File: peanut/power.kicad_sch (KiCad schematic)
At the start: 23 parts, among them J4 Battery JST, J5 Arming, Q5 PMOS, U2 TPS2116DRL, U3 LM3671MF

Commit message: Assigned some actual parts and footprints to symbols.
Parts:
- C10: renamed from C5; footprint (none) -> Capacitor_SMD:C_0402_1005Metric
- C11: renamed from C3; footprint (none) -> Capacitor_SMD:C_0402_1005Metric
- C12: renamed from C1; footprint (none) -> Capacitor_SMD:C_0402_1005Metric
- C13: renamed from C2; footprint (none) -> Capacitor_SMD:C_0402_1005Metric
- C9: renamed from C4; footprint (none) -> Capacitor_SMD:C_0402_1005Metric
- D5: footprint (none) -> LED_SMD:LED_0402_1005Metric
- J4: renamed from J5; footprint (none) -> TerminalBlock_Phoenix:TerminalBlock_Phoenix_MPT-0,5-2-2.54_1x02_P2.54mm_Horizontal
- R21: renamed from R14; footprint (none) -> Resistor_SMD:R_0402_1005Metric
- R22: renamed from R17; footprint (none) -> Resistor_SMD:R_0402_1005Metric
- R23: renamed from R15; footprint (none) -> Resistor_SMD:R_0402_1005Metric
- R24: renamed from R13; footprint (none) -> Resistor_SMD:R_0402_1005Metric
- R25: renamed from R16; footprint (none) -> Resistor_SMD:R_0402_1005Metric
- TP3: renamed from TP1; footprint (none) -> TestPoint:TestPoint_Pad_D1.0mm
- TP4: renamed from TP2; footprint (none) -> TestPoint:TestPoint_Pad_D1.0mm
- TP5: renamed from TP3; footprint (none) -> TestPoint:TestPoint_Pad_D1.0mm
- TP6: renamed from TP5; footprint (none) -> TestPoint:TestPoint_Pad_D1.0mm
- TP7: renamed from TP6; footprint (none) -> TestPoint:TestPoint_Pad_D1.0mm
- TP8: renamed from TP4; footprint (none) -> TestPoint:TestPoint_Pad_D1.0mm
- U4: renamed from U3; footprint Package_TO_SOT_SMD:TSOT-23-5 -> Package_LGA:LGA-8_3x5mm_P1.25mm
- U5: renamed from U2; footprint Package_TO_SOT_SMD:SOT-583-8 -> Package_DFN_QFN:QFN-32-1EP_5x5mm_P0.5mm_EP3.7x3.7mm
- renumbered J4 to J5, L1 to L2

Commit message: Footprint assignments for dual-channel NMOS; picked some more parts
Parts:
- D5: footprint LED_SMD:LED_0402_1005Metric -> LED_SMD:LED_0805_2012Metric; MPN (none) -> HSMG-C170
- Q5: footprint (none) -> Package_TO_SOT_SMD:SOT-23-3; MPN (none) -> SI2329DS-T1-GE3
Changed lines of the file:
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@@
 			)
 		)
-		(property "Footprint" ""
+		(property "Footprint" "Package_TO_SOT_SMD:SOT-23-3"
 			(at 189.23 66.04 0)
 			(effects
@@
 			)
 		)
-		(property "MPN" ""
+		(property "MPN" " SI2329DS-T1-GE3"
 			(at 191.77 71.12 90)
 			(effects
@@
 			)
 		)
-		(property "Footprint" "LED_SMD:LED_0402_1005Metric"
+		(property "Footprint" "LED_SMD:LED_0805_2012Metric"
 			(at 109.22 121.92 0)
 			(effects
@@
 			)
 		)
-		(property "MPN" ""
+		(property "MPN" " HSMG-C170"
 			(at 109.22 121.92 90)
 			(effects

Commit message: More component MPNs
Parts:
- C10: footprint Capacitor_SMD:C_0402_1005Metric -> Capacitor_SMD:C_0603_1608Metric; MPN (none) -> C1608X5R0J106K080AB
- C11, C12, C13: footprint Capacitor_SMD:C_0402_1005Metric -> Capacitor_SMD:C_0603_1608Metric; MPN (none) -> 06036C105MAT2A
- C9: footprint Capacitor_SMD:C_0402_1005Metric -> Capacitor_SMD:C_0603_1608Metric; MPN (none) -> CGA3E1X5R0J475K080AC
- D5: MPN HSMG-C170 -> HSMG-C170
- L2: MPN (none) -> LPO3310-222MLC
- Q5: MPN SI2329DS-T1-GE3 -> SI2329DS-T1-GE3
- R21, R22: MPN (none) -> SFR01MZPJ103
- R23: MPN (none) -> MR04X3302FTL
- R24, R25: MPN (none) -> 560112110231
- U4: footprint Package_LGA:LGA-8_3x5mm_P1.25mm -> Package_TO_SOT_SMD:TSOT-23-5; MPN (none) -> LM3671MF-3.3/NOPB
- U5: footprint Package_DFN_QFN:QFN-32-1EP_5x5mm_P0.5mm_EP3.7x3.7mm -> Package_TO_SOT_SMD:SOT-583-8; MPN (none) -> TPS2116DRLR
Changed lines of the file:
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@@
 			)
 		)
-		(property "Footprint" "Capacitor_SMD:C_0402_1005Metric"
+		(property "Footprint" "Capacitor_SMD:C_0603_1608Metric"
 			(at 111.4552 88.9 0)
 			(effects
@@
 			)
 		)
-		(property "MPN" ""
+		(property "MPN" "06036C105MAT2A"
 			(at 110.49 85.09 0)
 			(effects
@@
 			)
 		)
-		(property "MPN" ""
+		(property "MPN" "560112110231"
 			(at 80.01 134.62 0)
 			(effects
@@
 			)
 		)
-		(property "Footprint" "Package_DFN_QFN:QFN-32-1EP_5x5mm_P0.5mm_EP3.7x3.7mm"
+		(property "Footprint" "Package_TO_SOT_SMD:SOT-583-8"
 			(at 139.7 98.552 0)
 			(effects
@@
 			)
 		)
-		(property "MPN" ""
+		(property "MPN" "TPS2116DRLR"
 			(at 139.7 76.2 0)
 			(effects
@@
 			)
 		)
-		(property "MPN" ""
+		(property "MPN" "LPO3310-222MLC"
 			(at 77.47 68.58 90)
 			(effects
@@
 			)
 		)
-		(property "Footprint" "Capacitor_SMD:C_0402_1005Metric"
+		(property "Footprint" "Capacitor_SMD:C_0603_1608Metric"
 			(at 53.0352 76.2 0)
 			(effects
@@
 			)
 		)
-		(property "MPN" ""
+		(property "MPN" "CGA3E1X5R0J475K080AC"
 			(at 52.07 72.39 0)
 			(effects
@@
 			)
 		)
-		(property "MPN" ""
+		(property "MPN" "SFR01MZPJ103"
 			(at 74.93 119.38 90)
 			(effects
@@
 			)
 		)
-		(property "Footprint" "Capacitor_SMD:C_0402_1005Metric"
+		(property "Footprint" "Capacitor_SMD:C_0603_1608Metric"
 			(at 119.0752 78.74 0)
 			(effects
@@
 			)
 		)
-		(property "MPN" ""
+		(property "MPN" "06036C105MAT2A"
 			(at 118.11 74.93 0)
 			(effects
@@
 			)
 		)
-		(property "MPN" " SI2329DS-T1-GE3"
+		(property "MPN" "SI2329DS-T1-GE3"
 			(at 191.77 71.12 90)
 			(effects
@@
 			)
 		)
-		(property "Footprint" "Capacitor_SMD:C_0402_1005Metric"
+		(property "Footprint" "Capacitor_SMD:C_0603_1608Metric"
 			(at 87.3252 76.2 0)
 			(effects
@@
 			)
 		)
-		(property "MPN" ""
+		(property "MPN" "C1608X5R0J106K080AB"
 			(at 86.36 72.39 0)
 			(effects
@@
 			)
 		)
-		(property "MPN" ""
+		(property "MPN" "SFR01MZPJ103"
 			(at 163.83 77.47 0)
 			(effects
@@
 			)
 		)
-		(property "MPN" ""
+		(property "MPN" "560112110231"
 			(at 109.22 129.54 0)
 			(effects
@@
 			)
 		)
-		(property "MPN" ""
+		(property "MPN" "MR04X3302FTL"
 			(at 80.01 124.46 0)
 			(effects
@@
 			)
 		)
-		(property "Footprint" "Package_LGA:LGA-8_3x5mm_P1.25mm"
+		(property "Footprint" "Package_TO_SOT_SMD:TSOT-23-5"
 			(at 67.31 77.47 0)
 			(effects
@@
 			)
 		)
-		(property "MPN" ""
+		(property "MPN" "LM3671MF-3.3/NOPB"
 			(at 66.04 71.12 0)
 			(effects
@@
 			)
 		)
-		(property "Footprint" "Capacitor_SMD:C_0402_1005Metric"
+		(property "Footprint" "Capacitor_SMD:C_0603_1608Metric"
 			(at 154.6352 80.01 0)
 			(effects
@@
 			)
 		)
-		(property "MPN" ""
+		(property "MPN" "06036C105MAT2A"
 			(at 153.67 76.2 0)
 			(effects
@@
 			)
 		)
-		(property "MPN" " HSMG-C170"
+		(property "MPN" "HSMG-C170"
 			(at 109.22 121.92 90)
 			(effects

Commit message: feat: Finish schematic
This commit "completes" the schematic to the best of my foresight for
the moment. All components have BOM MPNs and footprints assigned. I have
double checked pins on the 40MHz clock and that pin assignments on the
MCU are valid. I have selected a chip antenna with high gain, added
decoupling capacitors to the MCU, picked out terminal blocks and
followed the Espressif schematic guide. A preliminary layout can be
made.
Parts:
- J3: renamed from J5; footprint (none) -> Connector_JST:JST_PH_S2B-PH-K_1x02_P2.00mm_Horizontal; MPN (none) -> S2B-PH-K-S(LF)(SN)(PP)
- J4: MPN (none) -> 1725656
- L3: renamed from L2; footprint (none) -> LPO3310-222MLC:LPO3310222MLC
- TP3, TP4, TP5, TP6, TP7, TP8: MPN (none) -> -
- renumbered C9 to C16, C10 to C17, C13 to C18, C11 to C19, C12 to C20, R22 to R21, R23 to R22, R25 to R23, R21 to R25
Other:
- note added: "600mA max draw"
- note removed: "600mA max draw Double check pinout & ref circuitry"

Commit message: feat: Initial layout
I have roughed out the initial PCB layout. It is wider than I'd like,
and not near a peanut shape. It appears the "start" and "panic" LEDs
never had pins assigned to them. I think I will replace the MCU RX & TX
with these instead, since I can still use the RX and TX as probe pads
that way.
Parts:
- Q5: symbol Simulation_SPICE:PMOS -> Transistor_FET:Q_PMOS_GSD
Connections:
- net BAT+: now also Q5.3 (D); no longer Q5.1 (D)
- net GND: now also Q5.1 (G); no longer Q5.2 (G)
- net VBAT: now also Q5.2 (S); no longer Q5.3 (S)
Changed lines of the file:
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@@
 	)
 	(symbol
-		(lib_id "Simulation_SPICE:PMOS")
+		(lib_id "Transistor_FET:Q_PMOS_GSD")
 		(at 191.77 71.12 90)
 		(unit 1)
@@
 		)
 		(property "Datasheet" "https://ngspice.sourceforge.io/docs/ngspice-html-manual/manual.xhtml#cha_MOSFETs"
-			(at 204.47 71.12 0)
+			(at 191.77 71.12 0)
 			(hide yes)
 			(show_name no)
@@
 			)
 		)
-		(property "Description" "P-MOSFET transistor, drain/source/gate"
+		(property "Description" "P-MOSFET transistor, gate/source/drain"
 			(at 191.77 71.12 0)
 			(hide yes)

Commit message: feat: Better layout
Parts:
- removed TP3: 3V3, TestPoint:TestPoint_Pad_D1.0mm, symbol Connector:TestPoint
- removed TP4: VBAT, TestPoint:TestPoint_Pad_D1.0mm, symbol Connector:TestPoint
- removed TP5: VUSB, TestPoint:TestPoint_Pad_D1.0mm, symbol Connector:TestPoint
- removed TP6: PWR_SRC, TestPoint:TestPoint_Pad_D1.0mm, symbol Connector:TestPoint
- removed TP7: BAT+, TestPoint:TestPoint_Pad_D1.0mm, symbol Connector:TestPoint
- removed TP8: GND, TestPoint:TestPoint_Pad_D1.0mm, symbol Connector:TestPoint
- renumbered C16 to C14, C17 to C15, C18 to C16, C19 to C17, C20 to C18, D5 to D4, R21 to R20, R22 to R21, R23 to R22, R24 to R23, R25 to R24
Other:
- note removed: "Test points"
- moved on the sheet: D4, R20, R21, R22, R23

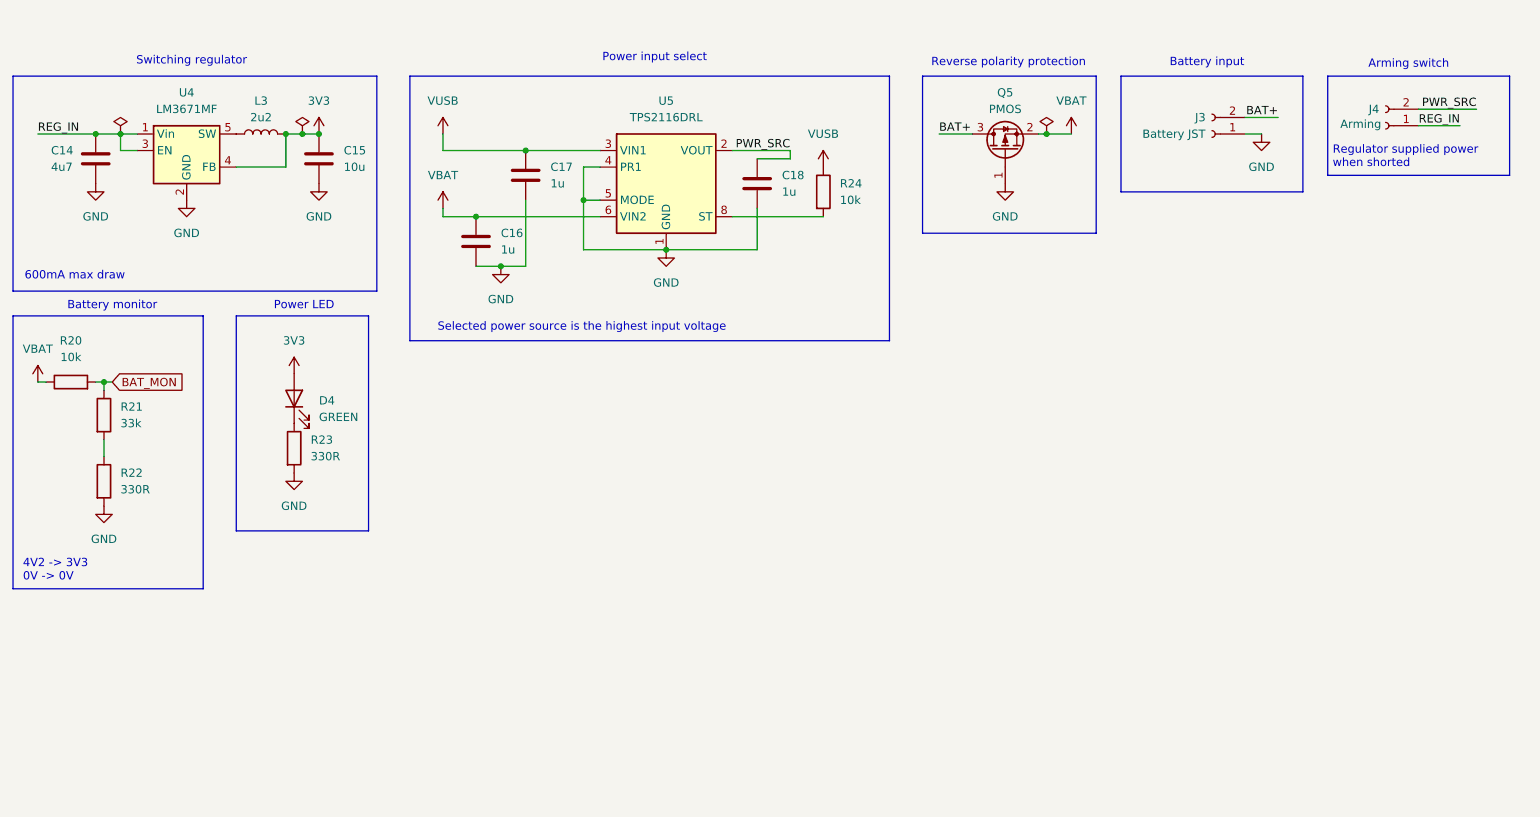
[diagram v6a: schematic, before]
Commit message: feat: Verify component features
Completed most of the review checklist for the initial revision. Routing
can commence once design rules are updated.
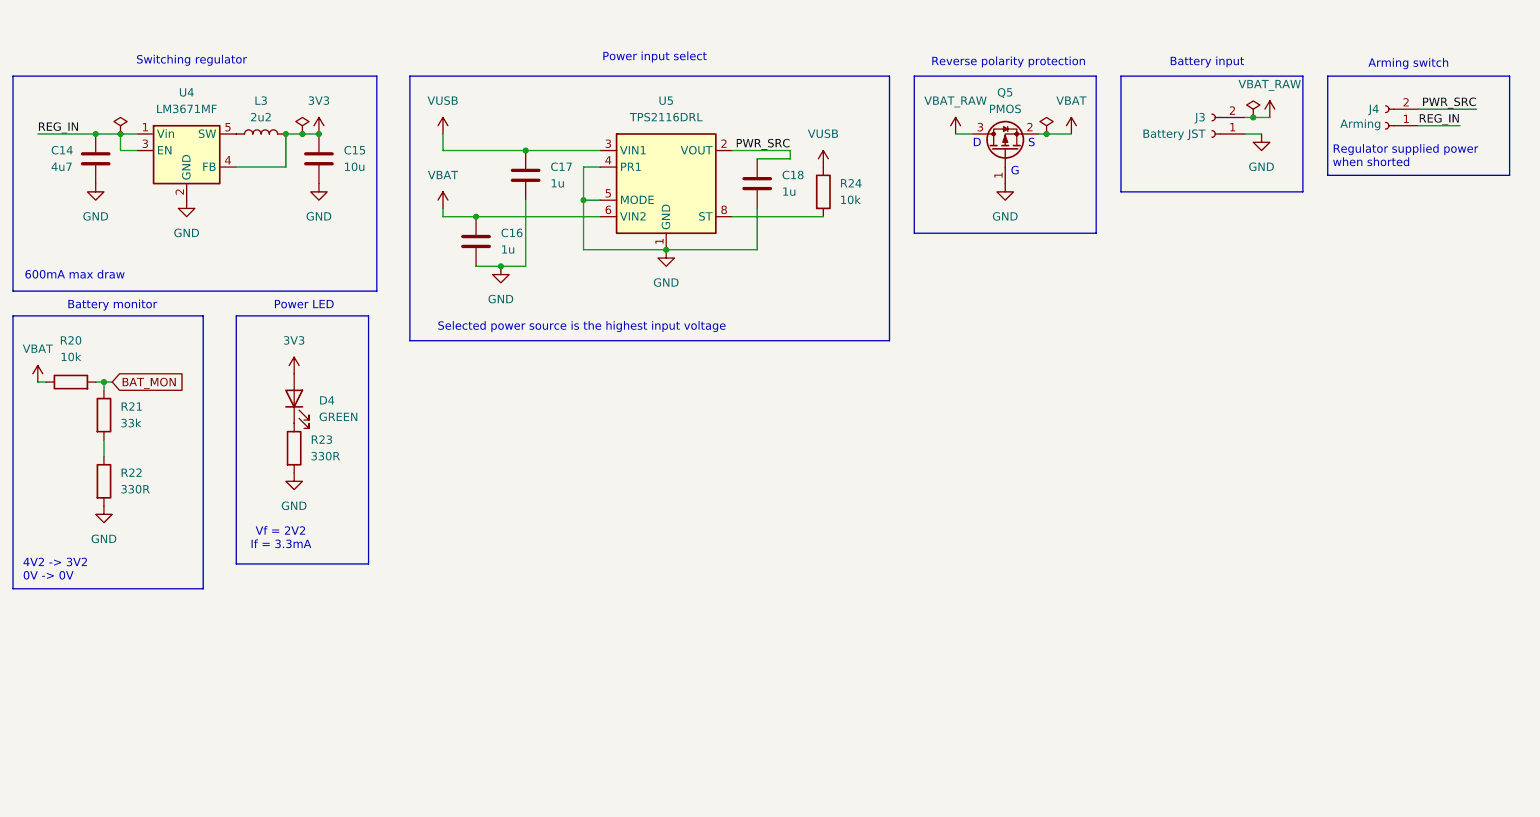
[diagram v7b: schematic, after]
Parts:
- Q5: footprint Package_TO_SOT_SMD:SOT-23-3 -> Package_TO_SOT_SMD:SOT-23
- U4: MPN LM3671MF-3.3/NOPB -> LM3671MFX-3.3/NOPB
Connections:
- net BAT+ renamed VBAT_RAW
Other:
- note added: "4V2 -> 3V2 0V -> 0V"
- note added: "D"
- note added: "G"
- note added: "S"
- note added: "Vf = 2V2 If = 3.3mA"
- note removed: "4V2 -> 3V3 0V -> 0V"

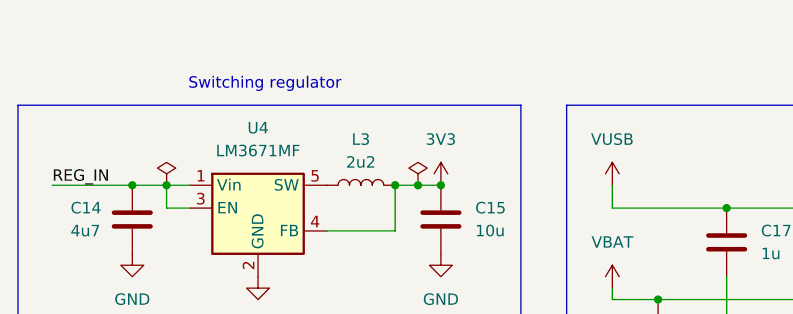
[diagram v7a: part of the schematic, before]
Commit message: feat: Cheaper inductor
Swapped inductor for one that is cheaper. Current board cost (minus JST
connector since that is not available on Mouser) is $44.76 CAD in
components.
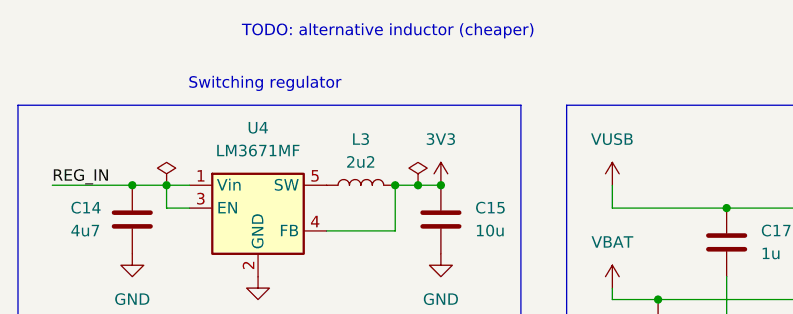
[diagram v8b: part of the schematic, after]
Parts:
- L3: footprint LPO3310-222MLC:LPO3310222MLC -> SRN3015BTA-2R2M:SRN3015BTA2R2M; MPN LPO3310-222MLC -> SRN3015BTA-2R2M
- R20, R24: MPN SFR01MZPJ103 -> MCS04020C1002FE000
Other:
- note added: "TODO: alternative inductor (cheaper)"
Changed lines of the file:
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@@
 		)
 	)
+	(text "TODO: alternative inductor (cheaper)"
+		(exclude_from_sim no)
+		(at 80.518 51.562 0)
+		(effects
+			(font
+				(size 1.27 1.27)
+			)
+		)
+	)
 	(text "4V2 -> 3V2\n0V -> 0V"
 		(exclude_from_sim no)
@@
 			)
 		)
-		(property "Footprint" "LPO3310-222MLC:LPO3310222MLC"
+		(property "Footprint" "SRN3015BTA-2R2M:SRN3015BTA2R2M"
 			(at 77.47 68.58 0)
 			(hide yes)
@@
 			)
 		)
-		(property "Datasheet" "https://www.mouser.ca/datasheet/3/995/1/lpo3310.pdf"
+		(property "Datasheet" "https://www.mouser.com/catalog/specsheets/Bourns_08042023_SRN3015BTA_datasheet.pdf"
 			(at 77.47 68.58 0)
 			(hide yes)
@@
 			)
 		)
-		(property "MPN" "LPO3310-222MLC"
+		(property "MPN" "SRN3015BTA-2R2M"
 			(at 77.47 68.58 90)
 			(hide yes)
@@
 			)
 		)
-		(property "MPN" "SFR01MZPJ103"
+		(property "MPN" "MCS04020C1002FE000"
 			(at 48.26 106.68 90)
 			(hide yes)
@@
 			)
 		)
-		(property "MPN" "SFR01MZPJ103"
+		(property "MPN" "MCS04020C1002FE000"
 			(at 163.83 77.47 0)
 			(hide yes)
